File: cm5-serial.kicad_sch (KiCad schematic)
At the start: 1 part

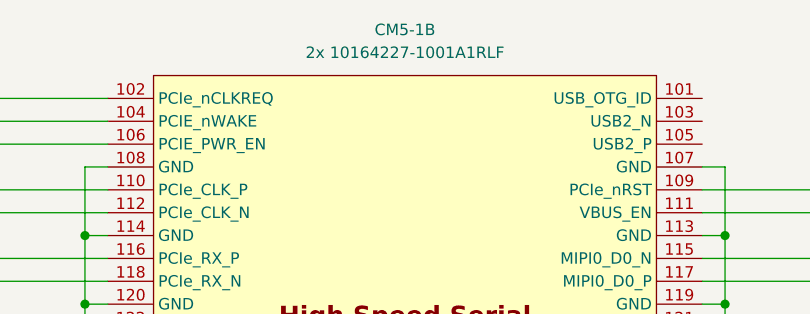
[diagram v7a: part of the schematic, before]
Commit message: redid gpio layout, removed one temp sensor, bom
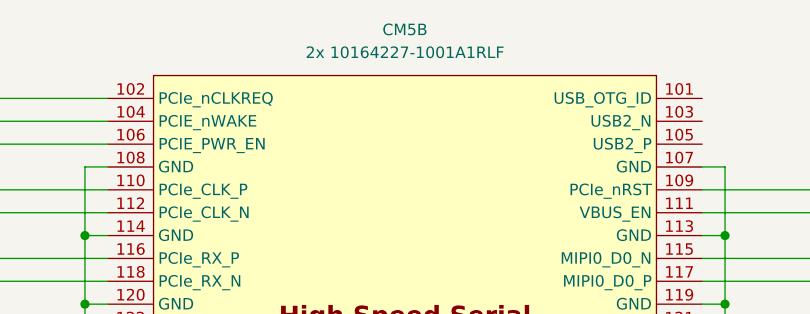
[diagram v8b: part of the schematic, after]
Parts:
- CM5: renamed from CM5-1; Manufacturer (none) -> Amphenol ICC (FCI); Manufacturer Product Number (none) -> 10164227-1001A1RLF
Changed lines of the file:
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@@
 		(dnp no)
 		(fields_autoplaced yes)
-		(property "Reference" "CM5-1"
+		(property "Reference" "CM5"
 			(at 116.84 21.59 0)
 			(effects
@@
 		)
 		(property "Description" ""
+			(at 116.84 91.44 0)
+			(effects
+				(font
+					(size 1.27 1.27)
+				)
+				(hide yes)
+			)
+		)
+		(property "Manufacturer" "Amphenol ICC (FCI)"
+			(at 116.84 91.44 0)
+			(effects
+				(font
+					(size 1.27 1.27)
+				)
+				(hide yes)
+			)
+		)
+		(property "Manufacturer Product Number" "10164227-1001A1RLF"
 			(at 116.84 91.44 0)
 			(effects
@@
 				)
 				(path "/40af415e-5e3a-41a5-ab07-08c2181863e4/0ab77a57-2cdd-42e3-9db1-21e8f0163da9/a16d2f87-5159-48aa-a50b-c816b9ab5677"
-					(reference "CM5-1")
+					(reference "CM5")
 					(unit 2)
 				)
